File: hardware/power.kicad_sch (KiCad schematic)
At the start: 19 parts, among them J16 BATT_12-48V, J17 12V_LINK, Q1 IRF9540N, U5 D36V50F5, U6 D36V50F12

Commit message: feat: board generation - placement DRC-clean (100x120, Pi stacks below, courtyard-verified)
Co-Authored-By: Claude Fable 5 <noreply@anthropic.com>
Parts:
- C3, C4: footprint Capacitor_THT:CP_Radial_D5.0mm_P2.00mm -> Capacitor_THT:CP_Radial_D6.3mm_P2.50mm
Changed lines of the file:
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@@
     (property "Value" "100u" (at 240.03 127 0)
       (effects (font (size 1.27 1.27))))
-    (property "Footprint" "Capacitor_THT:CP_Radial_D5.0mm_P2.00mm" (at 240.03 119.38 0)
+    (property "Footprint" "Capacitor_THT:CP_Radial_D6.3mm_P2.50mm" (at 240.03 119.38 0)
       (effects (font (size 1.27 1.27)) (hide yes)))
     (property "Datasheet" "" (at 240.03 119.38 0)
@@
     (property "Value" "100u/25V" (at 270.51 127 0)
       (effects (font (size 1.27 1.27))))
-    (property "Footprint" "Capacitor_THT:CP_Radial_D5.0mm_P2.00mm" (at 270.51 119.38 0)
+    (property "Footprint" "Capacitor_THT:CP_Radial_D6.3mm_P2.50mm" (at 270.51 119.38 0)
       (effects (font (size 1.27 1.27)) (hide yes)))
     (property "Datasheet" "" (at 270.51 119.38 0)

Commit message: feat: MPN table merged into schematic fields; SES import script
Co-Authored-By: Claude Fable 5 <noreply@anthropic.com>
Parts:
- C1, C2: MPN (none) -> EEU-FR1J471B
- C3, C4: MPN (none) -> EEU-FR1E101
- D4: MPN (none) -> BZX85C12-TAP
- D5: MPN (none) -> SMCJ58A
- F1: MPN (none) -> 3568
- J16, J17: MPN (none) -> CUI TB007-508-02
- Q1: MPN (none) -> IRF9540NPBF
- U5: MPN (none) -> Pololu 4091 (D36V50F5)
- U6: MPN (none) -> Pololu 4095 (D36V50F12)
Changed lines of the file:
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@@
     (property "Datasheet" "" (at 39.37 69.85 0)
       (effects (font (size 1.27 1.27)) (hide yes)))
+    (property "MPN" "CUI TB007-508-02" (at 39.37 69.85 0)
+      (effects (font (size 1.27 1.27)) (hide yes)))
     (pin "1")
     (pin "2")
@@
     (property "Datasheet" "" (at 69.85 69.85 0)
       (effects (font (size 1.27 1.27)) (hide yes)))
+    (property "MPN" "3568" (at 69.85 69.85 0)
+      (effects (font (size 1.27 1.27)) (hide yes)))
     (pin "1")
     (pin "2")
@@
       (effects (font (size 1.27 1.27)) (hide yes)))
     (property "Datasheet" "" (at 105.41 69.85 0)
+      (effects (font (size 1.27 1.27)) (hide yes)))
+    (property "MPN" "IRF9540NPBF" (at 105.41 69.85 0)
       (effects (font (size 1.27 1.27)) (hide yes)))
     (pin "1")
@@
     (property "Datasheet" "" (at 170.18 69.85 0)
       (effects (font (size 1.27 1.27)) (hide yes)))
+    (property "MPN" "BZX85C12-TAP" (at 170.18 69.85 0)
+      (effects (font (size 1.27 1.27)) (hide yes)))
     (pin "1")
     (pin "2")
@@
     (property "Datasheet" "" (at 199.39 69.85 0)
       (effects (font (size 1.27 1.27)) (hide yes)))
+    (property "MPN" "SMCJ58A" (at 199.39 69.85 0)
+      (effects (font (size 1.27 1.27)) (hide yes)))
     (pin "1")
     (pin "2")
@@
     (property "Datasheet" "" (at 229.87 69.85 0)
       (effects (font (size 1.27 1.27)) (hide yes)))
+    (property "MPN" "EEU-FR1J471B" (at 229.87 69.85 0)
+      (effects (font (size 1.27 1.27)) (hide yes)))
     (pin "1")
     (pin "2")
@@
     (property "Datasheet" "" (at 260.35 69.85 0)
       (effects (font (size 1.27 1.27)) (hide yes)))
+    (property "MPN" "EEU-FR1J471B" (at 260.35 69.85 0)
+      (effects (font (size 1.27 1.27)) (hide yes)))
     (pin "1")
     (pin "2")
@@
       (effects (font (size 1.27 1.27)) (hide yes)))
     (property "Datasheet" "" (at 69.85 119.38 0)
+      (effects (font (size 1.27 1.27)) (hide yes)))
+    (property "MPN" "Pololu 4091 (D36V50F5)" (at 69.85 119.38 0)
       (effects (font (size 1.27 1.27)) (hide yes)))
     (pin "1")
@@
     (property "Datasheet" "" (at 139.7 119.38 0)
       (effects (font (size 1.27 1.27)) (hide yes)))
+    (property "MPN" "Pololu 4095 (D36V50F12)" (at 139.7 119.38 0)
+      (effects (font (size 1.27 1.27)) (hide yes)))
     (pin "1")
     (pin "2")
@@
     (property "Datasheet" "" (at 199.39 119.38 0)
       (effects (font (size 1.27 1.27)) (hide yes)))
+    (property "MPN" "CUI TB007-508-02" (at 199.39 119.38 0)
+      (effects (font (size 1.27 1.27)) (hide yes)))
     (pin "1")
     (pin "2")
@@
     (property "Datasheet" "" (at 240.03 119.38 0)
       (effects (font (size 1.27 1.27)) (hide yes)))
+    (property "MPN" "EEU-FR1E101" (at 240.03 119.38 0)
+      (effects (font (size 1.27 1.27)) (hide yes)))
     (pin "1")
     (pin "2")
@@
     (property "Datasheet" "" (at 270.51 119.38 0)
       (effects (font (size 1.27 1.27)) (hide yes)))
-    (pin "1")
+    (property "MPN" "EEU-FR1E101" (at 270.51 119.38 0)
+      (effects (font (size 1.27 1.27)) (hide yes)))
+    (pin "1")

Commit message: feat: on-board 800W H-bridge (HIP4082 + 8 FET, ACS758, M5 lugs) + BTN8982 servo bridge; 160x120 board, placement DRC-clean
Co-Authored-By: Claude Fable 5 <noreply@anthropic.com>
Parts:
- removed J16: BATT_12-48V, TerminalBlock_CUI:TerminalBlock_CUI_TB007-508-02_1x02_P5.08mm_Horizontal, symbol Connector_Generic:Conn_01x02
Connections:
- net BATT_IN renamed VBAT_PWR
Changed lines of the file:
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@@
     (effects (font (size 2 2) (bold yes)) (justify left bottom))
-  )
-  (symbol (lib_id "Connector_Generic:Conn_01x02") (at 39.37 69.85 0) (unit 1)
-    (exclude_from_sim no) (in_bom yes) (on_board yes) (dnp no)
-    (property "Reference" "J16" (at 39.37 62.23 0)
-      (effects (font (size 1.27 1.27))))
-    (property "Value" "BATT_12-48V" (at 39.37 77.47 0)
-      (effects (font (size 1.27 1.27))))
-    (property "Footprint" "TerminalBlock_CUI:TerminalBlock_CUI_TB007-508-02_1x02_P5.08mm_Horizontal" (at 39.37 69.85 0)
-      (effects (font (size 1.27 1.27)) (hide yes)))
-    (property "Datasheet" "" (at 39.37 69.85 0)
-      (effects (font (size 1.27 1.27)) (hide yes)))
-    (property "MPN" "CUI TB007-508-02" (at 39.37 69.85 0)
-      (effects (font (size 1.27 1.27)) (hide yes)))
-    (pin "1")
-    (pin "2")
-    (instances (project "vanchor-helm" (path "/a0000000-0000-4000-8000-000000000001/c0000000-0000-4000-8000-000000000002" (reference "J16") (unit 1))))
   )
   (symbol (lib_id "Device:Fuse") (at 69.85 69.85 0) (unit 1)
@@
     (instances (project "vanchor-helm" (path "/a0000000-0000-4000-8000-000000000001/c0000000-0000-4000-8000-000000000002" (reference "#FLG02") (unit 1))))
   )
-  (label "BATT_IN" (at 34.29 69.85 180.0) (fields_autoplaced yes)
-    (effects (font (size 1.27 1.27)) (justify right))
-  )
-  (global_label "GND" (shape passive) (at 34.29 72.39 180.0) (fields_autoplaced yes)
-    (effects (font (size 1.27 1.27)) (justify right))
-    (property "Intersheetrefs" "${INTERSHEET_REFS}" (at 34.29 72.39 0)
-      (effects (font (size 1.27 1.27)) (hide yes)))
-  )
-  (label "BATT_IN" (at 69.85 66.04 90.0) (fields_autoplaced yes)
+  (global_label "VBAT_PWR" (shape passive) (at 69.85 66.04 90.0) (fields_autoplaced yes)
     (effects (font (size 1.27 1.27)) (justify left))
+    (property "Intersheetrefs" "${INTERSHEET_REFS}" (at 69.85 66.04 0)
+      (effects (font (size 1.27 1.27)) (hide yes)))
   )
   (label "VIN_RAW" (at 69.85 73.66 270.0) (fields_autoplaced yes)

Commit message: feat: routed board via scripted freerouting pipeline (T10) — known GUI touch-up items documented
Co-Authored-By: Claude Fable 5 <noreply@anthropic.com>
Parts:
- added J16: LOGIC 12-48V, TerminalBlock_CUI:TerminalBlock_CUI_TB007-508-02_1x02_P5.08mm_Horizontal, symbol Connector_Generic:Conn_01x02
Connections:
- net GND: now also J16.2 (Pin_2)
- net VBAT_PWR renamed BATT_IN
- net BATT_IN: now also J16.1 (Pin_1)
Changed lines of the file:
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@@
     (effects (font (size 2 2) (bold yes)) (justify left bottom))
+  )
+  (symbol (lib_id "Connector_Generic:Conn_01x02") (at 39.37 69.85 0) (unit 1)
+    (exclude_from_sim no) (in_bom yes) (on_board yes) (dnp no)
+    (property "Reference" "J16" (at 39.37 62.23 0)
+      (effects (font (size 1.27 1.27))))
+    (property "Value" "LOGIC 12-48V" (at 39.37 77.47 0)
+      (effects (font (size 1.27 1.27))))
+    (property "Footprint" "TerminalBlock_CUI:TerminalBlock_CUI_TB007-508-02_1x02_P5.08mm_Horizontal" (at 39.37 69.85 0)
+      (effects (font (size 1.27 1.27)) (hide yes)))
+    (property "Datasheet" "" (at 39.37 69.85 0)
+      (effects (font (size 1.27 1.27)) (hide yes)))
+    (pin "1")
+    (pin "2")
+    (instances (project "vanchor-helm" (path "/a0000000-0000-4000-8000-000000000001/c0000000-0000-4000-8000-000000000002" (reference "J16") (unit 1))))
   )
   (symbol (lib_id "Device:Fuse") (at 69.85 69.85 0) (unit 1)
@@
     (instances (project "vanchor-helm" (path "/a0000000-0000-4000-8000-000000000001/c0000000-0000-4000-8000-000000000002" (reference "#FLG02") (unit 1))))
   )
-  (global_label "VBAT_PWR" (shape passive) (at 69.85 66.04 90.0) (fields_autoplaced yes)
+  (label "BATT_IN" (at 34.29 69.85 180.0) (fields_autoplaced yes)
+    (effects (font (size 1.27 1.27)) (justify right))
+  )
+  (global_label "GND" (shape passive) (at 34.29 72.39 180.0) (fields_autoplaced yes)
+    (effects (font (size 1.27 1.27)) (justify right))
+    (property "Intersheetrefs" "${INTERSHEET_REFS}" (at 34.29 72.39 0)
+      (effects (font (size 1.27 1.27)) (hide yes)))
+  )
+  (label "BATT_IN" (at 69.85 66.04 90.0) (fields_autoplaced yes)
     (effects (font (size 1.27 1.27)) (justify left))
-    (property "Intersheetrefs" "${INTERSHEET_REFS}" (at 69.85 66.04 0)
-      (effects (font (size 1.27 1.27)) (hide yes)))
   )
   (label "VIN_RAW" (at 69.85 73.66 270.0) (fields_autoplaced yes)

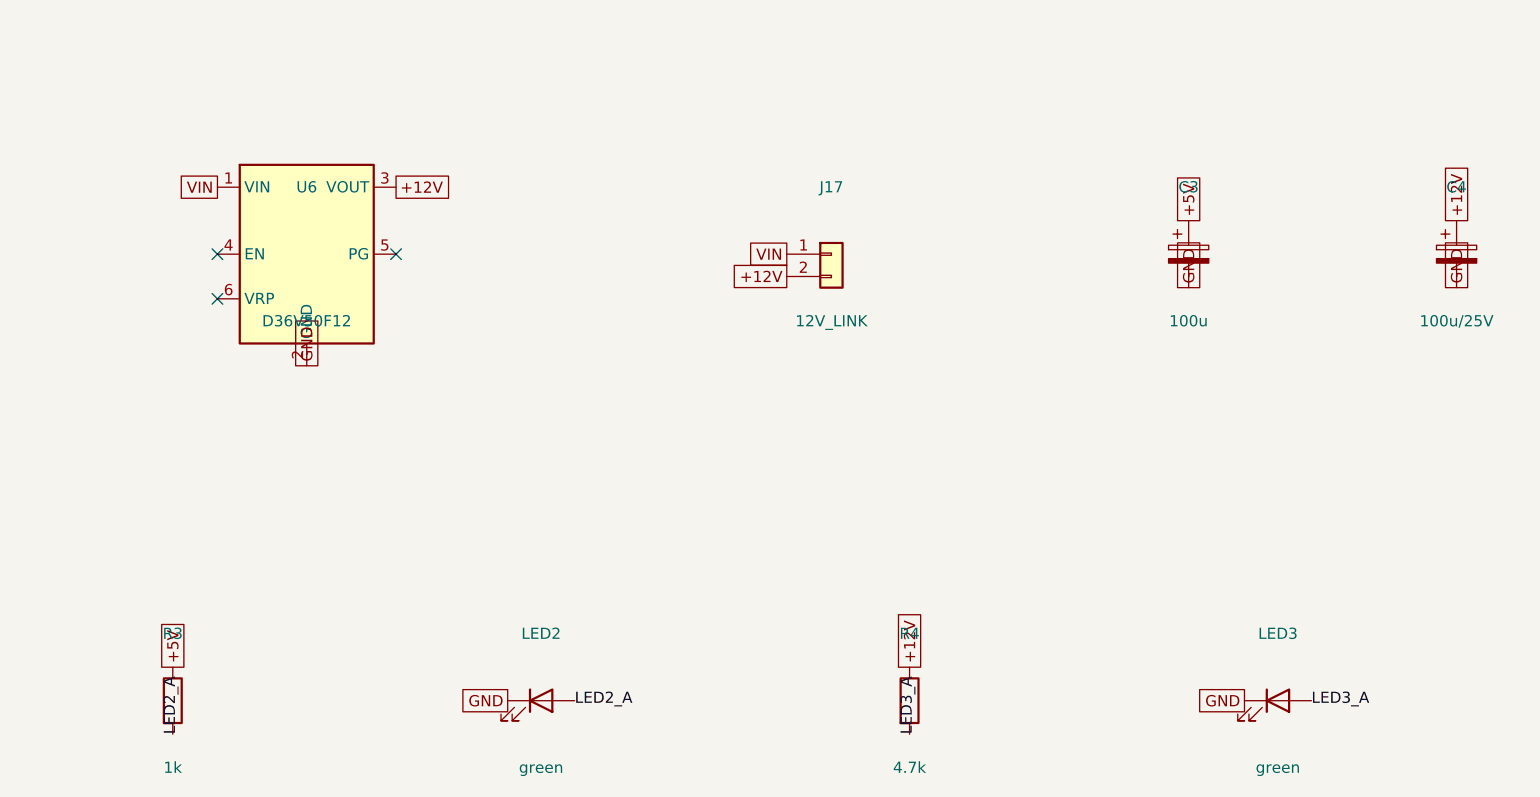
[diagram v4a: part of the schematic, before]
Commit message: cost pass 10 (schematic): remove on-board H-bridge, add J13 external-driver header (IBT-2 pinout); ERC 0, gate PASS
Co-Authored-By: Claude Fable 5 <noreply@anthropic.com>
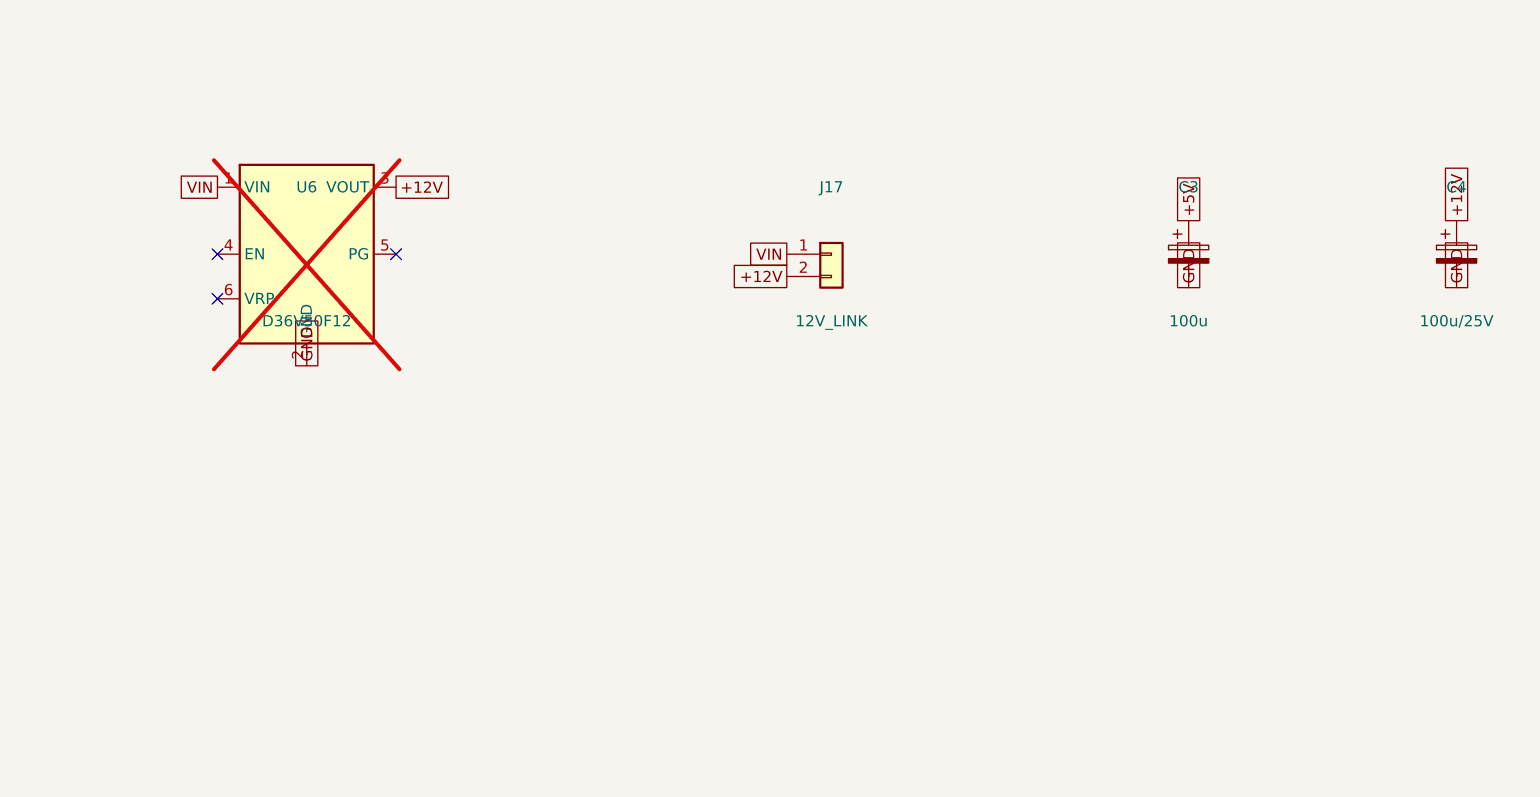
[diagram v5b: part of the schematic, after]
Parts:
- removed LED2, LED3: green, LED_THT:LED_D5.0mm, symbol Device:LED
- removed R3: 1k, Resistor_THT:R_Axial_DIN0207_L6.3mm_D2.5mm_P10.16mm_Horizontal, symbol Device:R
- removed R4: 4.7k, Resistor_THT:R_Axial_DIN0207_L6.3mm_D2.5mm_P10.16mm_Horizontal, symbol Device:R
- U6: now not fitted
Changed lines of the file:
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@@
   )
   (symbol (lib_id "vanchor-helm:D36V50Fx") (at 139.7 119.38 0) (unit 1)
-    (exclude_from_sim no) (in_bom yes) (on_board yes) (dnp no)
+    (exclude_from_sim no) (in_bom yes) (on_board yes) (dnp yes)
     (property "Reference" "U6" (at 139.7 111.76 0)
       (effects (font (size 1.27 1.27))))
@@
     (instances (project "vanchor-helm" (path "/a0000000-0000-4000-8000-000000000001/c0000000-0000-4000-8000-000000000002" (reference "LED1") (unit 1))))
   )
-  (symbol (lib_id "Device:R") (at 124.46 170.18 0) (unit 1)
-    (exclude_from_sim no) (in_bom yes) (on_board yes) (dnp no)
-    (property "Reference" "R3" (at 124.46 162.56 0)
-      (effects (font (size 1.27 1.27))))
-    (property "Value" "1k" (at 124.46 177.8 0)
-      (effects (font (size 1.27 1.27))))
-    (property "Footprint" "Resistor_THT:R_Axial_DIN0207_L6.3mm_D2.5mm_P10.16mm_Horizontal" (at 124.46 170.18 0)
-      (effects (font (size 1.27 1.27)) (hide yes)))
-    (property "Datasheet" "" (at 124.46 170.18 0)
-      (effects (font (size 1.27 1.27)) (hide yes)))
-    (pin "1")
-    (pin "2")
-    (instances (project "vanchor-helm" (path "/a0000000-0000-4000-8000-000000000001/c0000000-0000-4000-8000-000000000002" (reference "R3") (unit 1))))
-  )
-  (symbol (lib_id "Device:LED") (at 166.37 170.18 0) (unit 1)
-    (exclude_from_sim no) (in_bom yes) (on_board yes) (dnp no)
-    (property "Reference" "LED2" (at 166.37 162.56 0)
-      (effects (font (size 1.27 1.27))))
-    (property "Value" "green" (at 166.37 177.8 0)
-      (effects (font (size 1.27 1.27))))
-    (property "Footprint" "LED_THT:LED_D5.0mm" (at 166.37 170.18 0)
-      (effects (font (size 1.27 1.27)) (hide yes)))
-    (property "Datasheet" "" (at 166.37 170.18 0)
-      (effects (font (size 1.27 1.27)) (hide yes)))
-    (pin "1")
-    (pin "2")
-    (instances (project "vanchor-helm" (path "/a0000000-0000-4000-8000-000000000001/c0000000-0000-4000-8000-000000000002" (reference "LED2") (unit 1))))
-  )
-  (symbol (lib_id "Device:R") (at 208.28 170.18 0) (unit 1)
-    (exclude_from_sim no) (in_bom yes) (on_board yes) (dnp no)
-    (property "Reference" "R4" (at 208.28 162.56 0)
-      (effects (font (size 1.27 1.27))))
-    (property "Value" "4.7k" (at 208.28 177.8 0)
-      (effects (font (size 1.27 1.27))))
-    (property "Footprint" "Resistor_THT:R_Axial_DIN0207_L6.3mm_D2.5mm_P10.16mm_Horizontal" (at 208.28 170.18 0)
-      (effects (font (size 1.27 1.27)) (hide yes)))
-    (property "Datasheet" "" (at 208.28 170.18 0)
-      (effects (font (size 1.27 1.27)) (hide yes)))
-    (pin "1")
-    (pin "2")
-    (instances (project "vanchor-helm" (path "/a0000000-0000-4000-8000-000000000001/c0000000-0000-4000-8000-000000000002" (reference "R4") (unit 1))))
-  )
-  (symbol (lib_id "Device:LED") (at 250.19 170.18 0) (unit 1)
-    (exclude_from_sim no) (in_bom yes) (on_board yes) (dnp no)
-    (property "Reference" "LED3" (at 250.19 162.56 0)
-      (effects (font (size 1.27 1.27))))
-    (property "Value" "green" (at 250.19 177.8 0)
-      (effects (font (size 1.27 1.27))))
-    (property "Footprint" "LED_THT:LED_D5.0mm" (at 250.19 170.18 0)
-      (effects (font (size 1.27 1.27)) (hide yes)))
-    (property "Datasheet" "" (at 250.19 170.18 0)
-      (effects (font (size 1.27 1.27)) (hide yes)))
-    (pin "1")
-    (pin "2")
-    (instances (project "vanchor-helm" (path "/a0000000-0000-4000-8000-000000000001/c0000000-0000-4000-8000-000000000002" (reference "LED3") (unit 1))))
-  )
   (symbol (lib_id "power:PWR_FLAG") (at 292.1 170.18 0) (unit 1)
     (exclude_from_sim no) (in_bom yes) (on_board yes) (dnp no)
@@
       (effects (font (size 1.27 1.27)) (hide yes)))
   )
-  (global_label "+5V" (shape passive) (at 124.46 166.37 90.0) (fields_autoplaced yes)
-    (effects (font (size 1.27 1.27)) (justify left))
-    (property "Intersheetrefs" "${INTERSHEET_REFS}" (at 124.46 166.37 0)
-      (effects (font (size 1.27 1.27)) (hide yes)))
-  )
-  (label "LED2_A" (at 124.46 173.99 270.0) (fields_autoplaced yes)
-    (effects (font (size 1.27 1.27)) (justify left))
-  )
-  (label "LED2_A" (at 170.18 170.18 0.0) (fields_autoplaced yes)
-    (effects (font (size 1.27 1.27)) (justify left))
-  )
-  (global_label "GND" (shape passive) (at 162.56 170.18 180.0) (fields_autoplaced yes)
-    (effects (font (size 1.27 1.27)) (justify right))
-    (property "Intersheetrefs" "${INTERSHEET_REFS}" (at 162.56 170.18 0)
-      (effects (font (size 1.27 1.27)) (hide yes)))
-  )
-  (global_label "+12V" (shape passive) (at 208.28 166.37 90.0) (fields_autoplaced yes)
-    (effects (font (size 1.27 1.27)) (justify left))
-    (property "Intersheetrefs" "${INTERSHEET_REFS}" (at 208.28 166.37 0)
-      (effects (font (size 1.27 1.27)) (hide yes)))
-  )
-  (label "LED3_A" (at 208.28 173.99 270.0) (fields_autoplaced yes)
-    (effects (font (size 1.27 1.27)) (justify left))
-  )
-  (label "LED3_A" (at 254 170.18 0.0) (fields_autoplaced yes)
-    (effects (font (size 1.27 1.27)) (justify left))
-  )
-  (global_label "GND" (shape passive) (at 246.38 170.18 180.0) (fields_autoplaced yes)
-    (effects (font (size 1.27 1.27)) (justify right))
-    (property "Intersheetrefs" "${INTERSHEET_REFS}" (at 246.38 170.18 0)
-      (effects (font (size 1.27 1.27)) (hide yes)))
-  )
